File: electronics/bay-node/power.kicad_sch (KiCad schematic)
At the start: 23 parts, among them J1 ROW IN, J2 ROW OUT, Q1 SUD50P06-15(UMW), U1 LMR51635YDDCR, U2 AMS1117-3.3

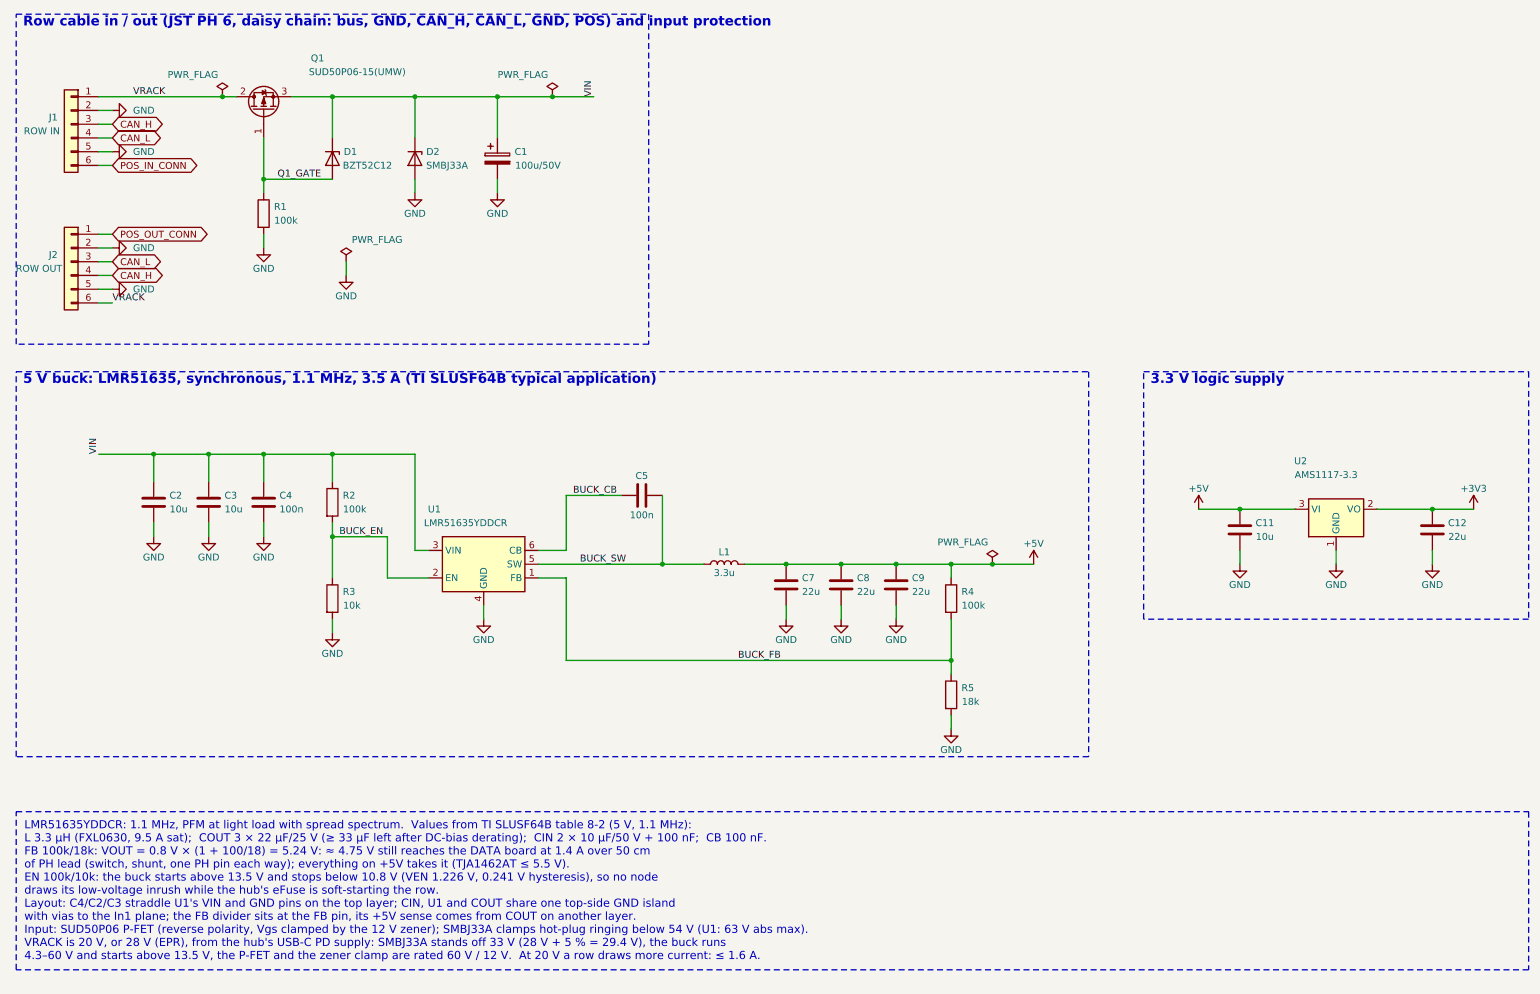
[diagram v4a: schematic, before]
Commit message: Node 5 V buck: LMR51625 with TI's 4.7 µH
The bay node's U1 goes from the LMR51635YDDCR (3.5 A) to its 2.5 A
sibling, the LMR51625YDDCR (C44991044), as the user asked.  TI SLUSF64B
covers both parts: they have the same DDC package and pinout (FB 1,
EN 2, VIN 3, GND 4, SW 5, CB 6), the same 0.8 V reference, the same EN
thresholds and the same 63 V absolute maximum.

L1 goes to 4.7 µH, per SLUSF64B table 8-1 (LMR51625, 5 V, 1.1 MHz).
The new part is the FXL0630-4R7-M (C167220), in the same footprint:
9 A saturation, 6 A rms, 33 mΩ.  The existing 3 × 22 µF output meets
the table's 22 µF.

Current headroom: a bay draws at most 2.2 A (node 0.30 A, the DUT
switch's 1.52 A, camera 0.36 A).  From 28 V the inductor then peaks at
about 2.6 A (0.8 A ripple), under the 2.5 A part's 2.9 A minimum peak
limit.  With 3.3 µH the peak would be 2.74 A.

The hub keeps the LMR51635 under the "buck" catalogue key.  The node
uses two new keys, "buck25" and "buck_l47".

CPL: JLC's EasyEDA footprint of C44991044 is pad for pad that of
C45262770 and C7519, so it gets the same 270° correction.  C167220
shares C167219's footprint and needs no correction.

Board: schematic regenerated; the routed PCB keeps its routing (only
U1 and L1 properties change, copied from a fresh build).  ERC 0,
DRC 0, unconnected 0, parity 0.  Gerbers, CPL and renders unchanged.

Cost:
- node order $322.96 -> $316.95 (-$6.01 components: LCSC $1.0744
  against $1.5997 at 10, the inductor $0.096 against $0.107, × 1.12);
- one rack's JLC boards $752.95 -> $746.43 (5 racks $310.59,
  10 racks $257.85);
- BOM total €1,013 -> €1,007 (€126 a bay);
- the 9-instead-of-10 lever is now $2.34.

The parts snapshot gains the two parts.  The BOM note prints a
negative adjustment as "− $6.01", not "+ $-6.01".

Co-Authored-By: Claude Opus 5.5 <noreply@anthropic.com>
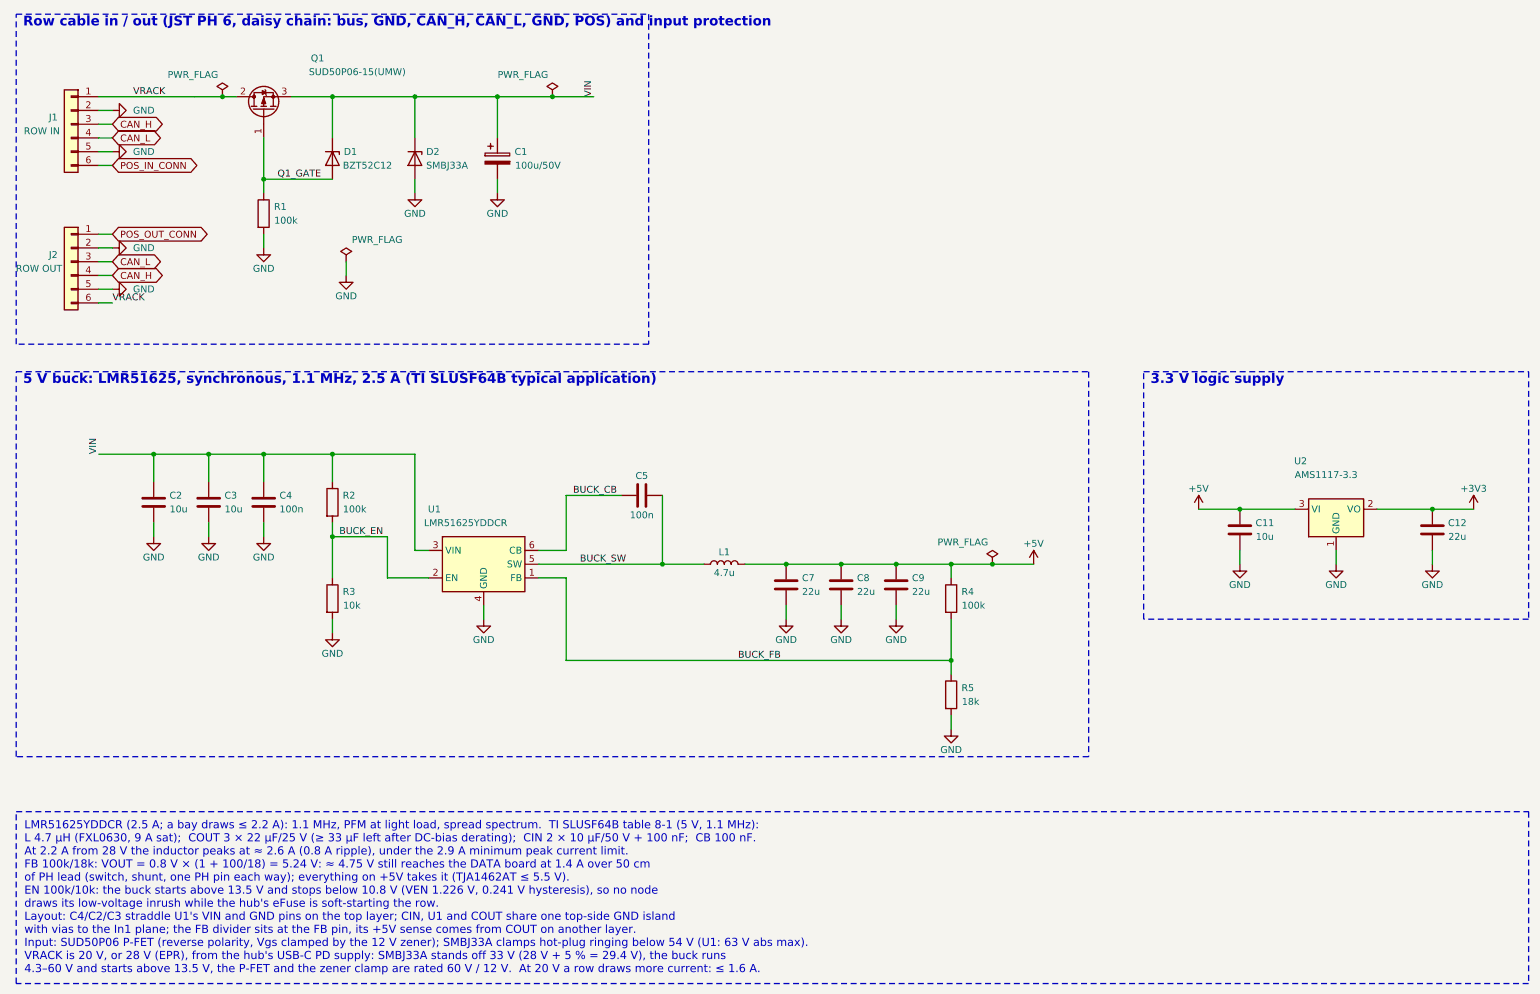
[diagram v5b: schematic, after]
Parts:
- L1: value 3.3u -> 4.7u; LCSC C167219 -> C167220; MPN FXL0630-3R3-M -> FXL0630-4R7-M
- U1: value LMR51635YDDCR -> LMR51625YDDCR; Alternative LMR51635YFDDCR (C44750836): same, forced PWM, no spread spe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 -> LMR51625YFDDCR (C45262768): same, forced PWM, no spread spe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; LCSC C45262770 -> C44991044; MPN LMR51635YDDCR -> LMR51625YDDCR
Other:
- note added: "5 V buck: LMR51625, synchronous, 1.1 MHz, 2.5 A (TI SLUSF64B typical application)"
- note removed: "5 V buck: LMR51635, synchronous, 1.1 MHz, 3.5 A (TI SLUSF64B typical application)"
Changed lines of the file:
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@@
 			)
 		)
-		(property "Value" "LMR51635YDDCR"
+		(property "Value" "LMR51625YDDCR"
 			(at 98.265 109.22 0)
 			(effects
@@
 			)
 		)
-		(property "Datasheet" "https://www.ti.com/lit/ds/symlink/lmr51635.pdf"
+		(property "Datasheet" "https://www.ti.com/lit/ds/symlink/lmr51625.pdf"
 			(at 101.6 116.84 0)
 			(effects
@@
 			)
 		)
-		(property "Description" "4.3–60 V 3.5 A synchronous buck, 1.1 MHz, PFM + spread spectrum"
+		(property "Description" "4.3–60 V 2.5 A synchronous buck, 1.1 MHz, PFM + spread spectrum"
 			(at 101.6 116.84 0)
 			(effects
@@
 			)
 		)
-		(property "MPN" "LMR51635YDDCR"
+		(property "MPN" "LMR51625YDDCR"
 			(at 101.6 116.84 0)
 			(effects
@@
 			)
 		)
-		(property "LCSC" "C45262770"
+		(property "LCSC" "C44991044"
 			(at 101.6 116.84 0)
 			(effects
@@
 			)
 		)
-		(property "Alternative" "LMR51635YFDDCR (C44750836): same, forced PWM, no spread spectrum"
+		(property "Alternative" "LMR51625YFDDCR (C45262768): same, forced PWM, no spread spectrum; LMR51635YDDCR (C45262770): 3.5 A, 3.3 µH"
 			(at 101.6 116.84 0)
 			(effects
@@
 			)
 		)
-		(property "Value" "3.3u"
+		(property "Value" "4.7u"
 			(at 146.05 118.44 90)
 			(effects
@@
 			)
 		)
-		(property "Description" "3.3 µH, 9.5 A sat, 8.5 A rms, 22 mΩ, molded"
+		(property "Description" "4.7 µH, 9 A sat, 6 A rms, 33 mΩ, molded"
 			(at 146.05 116.84 0)
 			(effects
@@
 			)
 		)
-		(property "MPN" "FXL0630-3R3-M"
+		(property "MPN" "FXL0630-4R7-M"
 			(at 146.05 116.84 0)
 			(effects
@@
 			)
 		)
-		(property "LCSC" "C167219"
+		(property "LCSC" "C167220"
 			(at 146.05 116.84 0)
 			(effects
@@
 		)
 	)
-	(text "5 V buck: LMR51635, synchronous, 1.1 MHz, 3.5 A (TI SLUSF64B typical application)"
+	(text "5 V buck: LMR51625, synchronous, 1.1 MHz, 2.5 A (TI SLUSF64B typical application)"
 		(exclude_from_sim no)
 		(at 16.51 83.82 0)
@@
 		)
 	)
-	(text_box "LMR51635YDDCR: 1.1 MHz, PFM at light load with spread spectrum.  Values from TI SLUSF64B table 8-2 (5 V, 1.1 MHz):\n  L 3.3 µH (FXL0630, 9.5 A sat);  COUT 3 × 22 µF/25 V (≥ 33 µF left after DC-bias derating);  CIN 2 × 10 µF/50 V + 100 nF;  CB 100 nF.\nFB 100k/18k: VOUT = 0.8 V × (1 + 100/18) = 5.24 V: ≈ 4.75 V still reaches the DATA board at 1.4 A over 50 cm\n  of PH lead (switch, shunt, one PH pin each way); everything on +5V takes it (TJA1462AT ≤ 5.5 V).\nEN 100k/10k: the buck starts above 13.5 V and stops below 10.8 V (VEN 1.226 V, 0.241 V hysteresis), so no node\n  draws its low-voltage inrush while the hub's eFuse is soft-starting the row.\nLayout: C4/C2/C3 straddle U1's VIN and GND pins on the top layer; CIN, U1 and COUT share one top-side GND island\n  with vias to the In1 plane; the FB divider sits at the FB pin, its +5V sense comes from COUT on another layer.\nInput: SUD50P06 P-FET (reverse polarity, Vgs clamped by the 12 V zener); SMBJ33A clamps hot-plug ringing below 54 V (U1: 63 V abs max).\nVRACK is 20 V, or 28 V (EPR), from the hub's USB-C PD supply: SMBJ33A stands off 33 V (28 V + 5 % = 29.4 V), the buck runs\n  4.3–60 V and starts above 13.5 V, the P-FET and the zener clamp are rated 60 V / 12 V.  At 20 V a row draws more current: ≤ 1.6 A."
+	(text_box "LMR51625YDDCR (2.5 A; a bay draws ≤ 2.2 A): 1.1 MHz, PFM at light load, spread spectrum.  TI SLUSF64B table 8-1 (5 V, 1.1 MHz):\n  L 4.7 µH (FXL0630, 9 A sat);  COUT 3 × 22 µF/25 V (≥ 33 µF left after DC-bias derating);  CIN 2 × 10 µF/50 V + 100 nF;  CB 100 nF.\n  At 2.2 A from 28 V the inductor peaks at ≈ 2.6 A (0.8 A ripple), under the 2.9 A minimum peak current limit.\nFB 100k/18k: VOUT = 0.8 V × (1 + 100/18) = 5.24 V: ≈ 4.75 V still reaches the DATA board at 1.4 A over 50 cm\n  of PH lead (switch, shunt, one PH pin each way); everything on +5V takes it (TJA1462AT ≤ 5.5 V).\nEN 100k/10k: the buck starts above 13.5 V and stops below 10.8 V (VEN 1.226 V, 0.241 V hysteresis), so no node\n  draws its low-voltage inrush while the hub's eFuse is soft-starting the row.\nLayout: C4/C2/C3 straddle U1's VIN and GND pins on the top layer; CIN, U1 and COUT share one top-side GND island\n  with vias to the In1 plane; the FB divider sits at the FB pin, its +5V sense comes from COUT on another layer.\nInput: SUD50P06 P-FET (reverse polarity, Vgs clamped by the 12 V zener); SMBJ33A clamps hot-plug ringing below 54 V (U1: 63 V abs max).\nVRACK is 20 V, or 28 V (EPR), from the hub's USB-C PD supply: SMBJ33A stands off 33 V (28 V + 5 % = 29.4 V), the buck runs\n  4.3–60 V and starts above 13.5 V, the P-FET and the zener clamp are rated 60 V / 12 V.  At 20 V a row draws more current: ≤ 1.6 A."
 		(exclude_from_sim no)
 		(at 15.24 162.56 0)
-		(size 279.4 29.21)
+		(size 279.4 31.75)
 		(margins 1.5 1.5 1.5 1.5)
 		(stroke

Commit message: Bay node: AP2114H for the 3.3 V, camera ESD clamped to +3V3
The schematic counter-review's fixes, approved by the user.

- U2: AP2114H-3.3TRG1 (C150716, catalog ldo_1a) instead of the AMS1117-3.3.
  It is specified stable with ceramics (C11, C12); the AMS1117 guarantees it
  only with 22 uF tantalum.  Same SOT-223 "H" pinout (1 GND, 2 and tab VOUT,
  3 VIN), footprint and copper: only the part's properties change.
- U12, U13 (USBLC6 on the camera lead): pin 5 on +3V3 instead of CAM_5V.
  With CAM_5V off (the PTC tripped), the SPI lines would feed the pod through
  the upper diodes, and CAM_5V's clamp sits above the ESP32's 3.6 V.  A
  minimal patch of the routing, no re-route: the CAM_5V stub that only
  reached the two pins goes (10 segments); U12.5 gets a +3V3 feed to a via in
  In2's +3V3 area; U13.5, with no room for its own, joins U12.5 along the
  stub's old east path at 0.25 mm.  The straightening pass ran on +3V3 and
  CAM_5V.
- Stale notes: AUX_VREF goes through R23's 1k, not 33 ohms; the next node's
  pull-down is R29's 470k, not 100k.
- pcbgen.fanout_pads takes `only` (REF.PAD), to fan out a few pads of a
  routed board.

ERC 0, DRC 0, unconnected 0, parity 0, every 3D model found.  The renders,
Gerbers and viewer model are regenerated (the unchanged iso render kept).
The schematic, the BOM and the docs (the node table, the CPL fix table, the
bring-up check, PCBA review N9) follow.  The hub and bom/ are untouched.

Co-Authored-By: Claude Opus 5.5 <noreply@anthropic.com>
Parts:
- U2: value AMS1117-3.3 -> AP2114H-3.3TRG1; LCSC C6186 -> C150716; MPN AMS1117-3.3 -> AP2114H-3.3TRG1; Manufacturer AMS -> Diodes Incorporated
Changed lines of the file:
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@@
 			)
 		)
-		(property "Value" "AMS1117-3.3"
-			(at 257.235 100.33 0)
+		(property "Value" "AP2114H-3.3TRG1"
+			(at 259.335 100.33 0)
 			(effects
 				(font
@@
 			)
 		)
-		(property "Datasheet" ""
+		(property "Datasheet" "https://www.diodes.com/assets/Datasheets/AP2114.pdf"
 			(at 259.08 106.68 0)
 			(effects
@@
 			)
 		)
-		(property "Description" "3.3 V 1 A LDO"
+		(property "Description" "3.3 V 1 A LDO, 450 mV dropout at 1 A, SOT-223"
 			(at 259.08 106.68 0)
 			(effects
@@
 			)
 		)
-		(property "MPN" "AMS1117-3.3"
+		(property "MPN" "AP2114H-3.3TRG1"
 			(at 259.08 106.68 0)
 			(effects
@@
 			)
 		)
-		(property "Manufacturer" "AMS"
+		(property "Manufacturer" "Diodes Incorporated"
 			(at 259.08 106.68 0)
 			(effects
@@
 			)
 		)
-		(property "LCSC" "C6186"
+		(property "LCSC" "C150716"
 			(at 259.08 106.68 0)
 			(effects
